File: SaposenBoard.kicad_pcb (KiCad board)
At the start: 2 copper layers, 60 x 50 mm, 85 parts, among them IC1 BSO220, IC2 BSO220, IC3 BSO220, IC4 BSO220, J1 ADC, J2 ADC/Servo, J3 I2C, J4 ADC_Extend, J5 Encoder1, J6 Encoder2, J7 Motor1, J8 Motor2, J9 Battery, Q1 BSS138, Q2 BSS138, Q3 BSS138, Q4 BSS138, Q5 BSS138, Q6 BSS138, Q7 BSS138, SW2 SW, SW3 BatterySW, U1 74CBTLV3257, U4 A4955GLPTR-T, U5 A4955GLPTR-T, U6 NUCLEO-F303K8, U7 MPU-6500

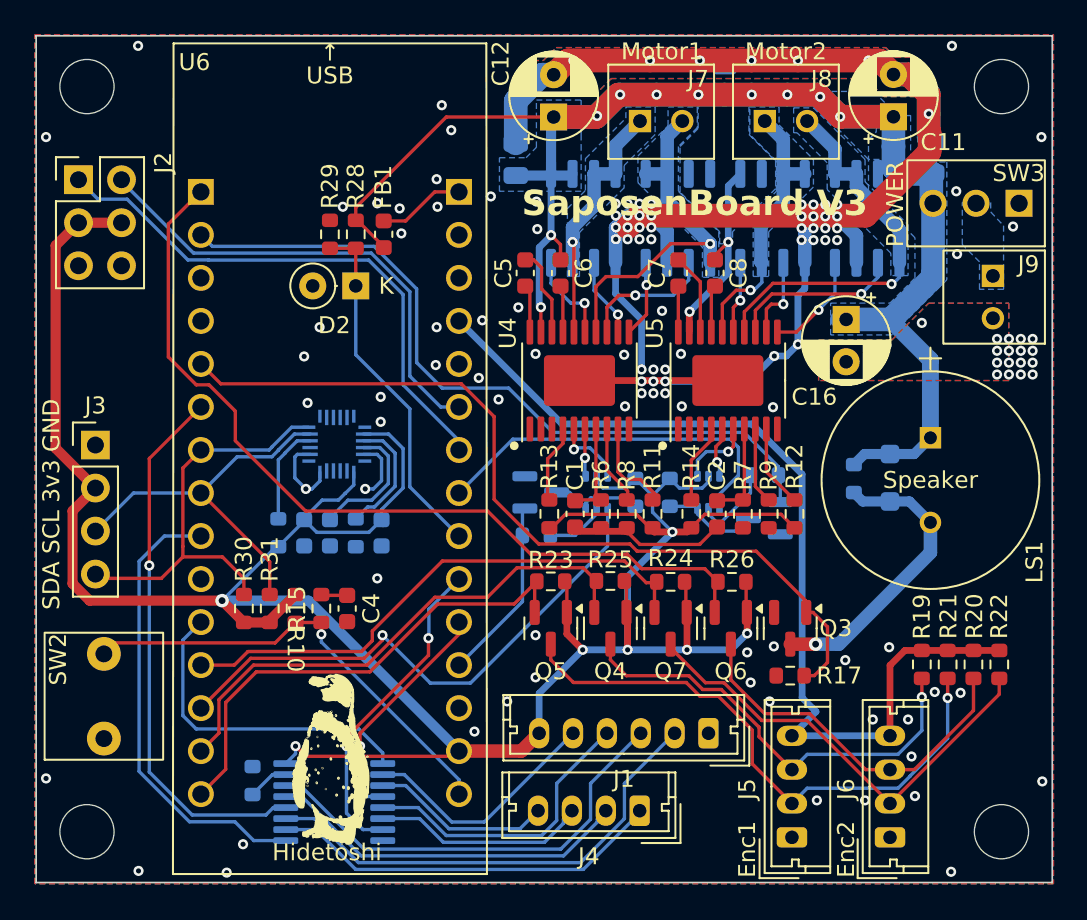
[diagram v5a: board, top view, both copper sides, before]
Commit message: [update]フットプリントを調整
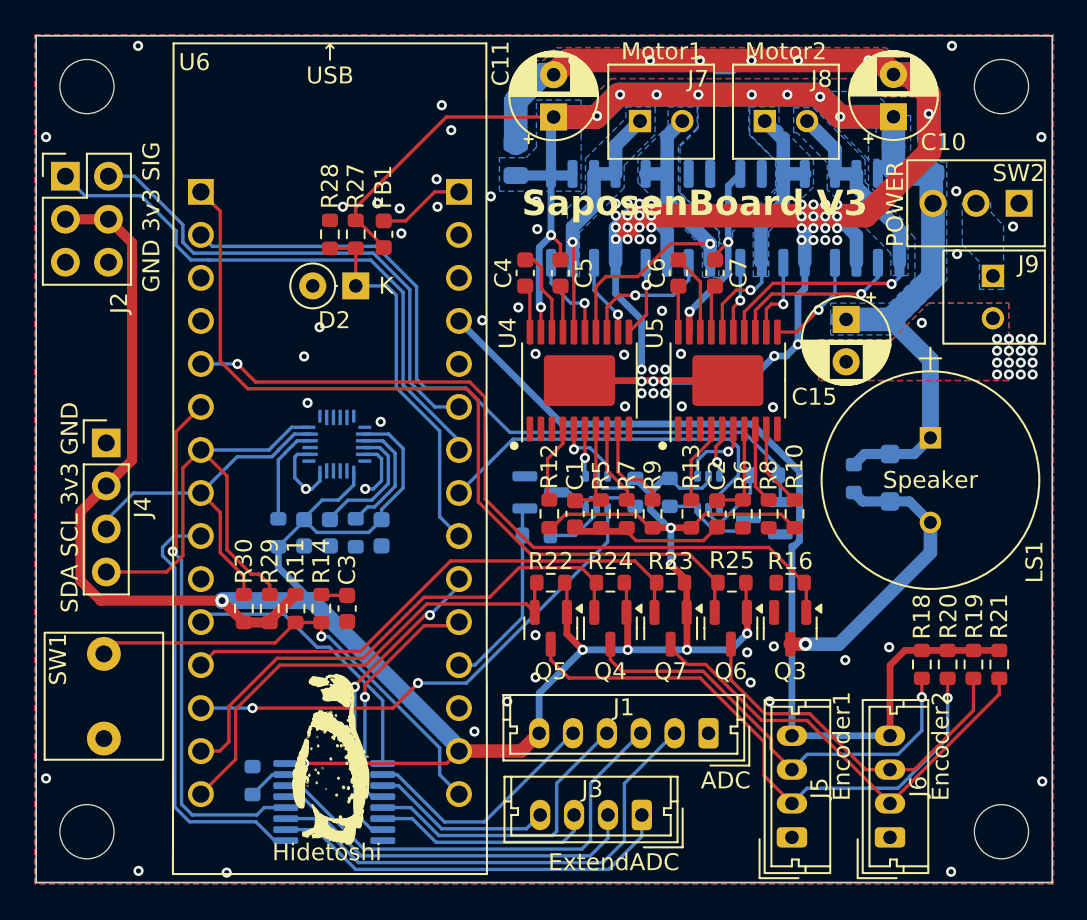
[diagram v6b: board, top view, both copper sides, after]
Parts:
- moved R16 5.49 mm to (144.5, 82.3)
- moved R29 1.52 mm to (113.8, 83.8)
- moved R30 1.52 mm to (112.3, 83.8)
- moved J2 0.80 mm to (101.7, 58.3)
- moved J4 0.65 mm to (104.1, 74.0)
- moved J3 0.28 mm to (135.8, 96.0)
- moved R24 0.10 mm to (133.9, 82.3)
- moved R22 0.08 mm to (130.4, 82.3)
- moved R23 0.05 mm to (137.5, 82.3)
- moved R25 0.05 mm to (141.1, 82.3)
- renumbered C11 to C10, C12 to C11, C13 to C12, C14 to C13, C15 to C14, C16 to C15, C17 to C16, C4 to C3, C5 to C4, C6 to C5, C7 to C6, C8 to C7, C9 to C8, C10 to C9, J4 to J3, J3 to J4, R12 to R10, R10 to R11, R13 to R12, R14 to R13, R15 to R14, R16 to R15, R17 to R16, R18 to R17, R19 to R18, R20 to R19, R21 to R20, R22 to R21, R23 to R22, R24 to R23, R25 to R24, R26 to R25, R27 to R26, R28 to R27, R29 to R28, R30 to R29, R31 to R30, R32 to R31, R6 to R5, R7 to R6, R8 to R7, R9 to R8, R11 to R9, SW2 to SW1, SW3 to SW2
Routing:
- net +3V3: track 167.7 -> 160.8 mm, vias 7 -> 8
- net /SDA: track 24.9 -> 30.0 mm
- net /SPEAKER: track 50.5 -> 46.3 mm, vias 0 -> 1
- net /MOT1_PH: track 32.7 -> 30.1 mm, vias 1 -> 2
- net /ADC_SEL: track 19.3 -> 16.8 mm
- net /ADC2_1: track 28.5 -> 30.2 mm
- net /ADC4: track 27.0 -> 25.6 mm
- net /ADC2_2: track 32.5 -> 33.9 mm
- net /SCLK: track 23.0 -> 21.7 mm
- net /ADC3: track 32.1 -> 31.0 mm
- net /ENC1_2: track 29.2 -> 28.1 mm
- net Net-(D2-K): track 21.0 -> 22.1 mm
- net /ENC2_1: track 51.4 -> 50.6 mm
- net /Sensor1_4: track 28.4 -> 29.2 mm
- net /Sensor1_3: track 26.6 -> 27.3 mm
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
